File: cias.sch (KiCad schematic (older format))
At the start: 60 parts, among them CN13 KEYBOARD, CN6 DB25_Male, CN7 DB25_Female, Q501 2N3904, Q502 2N3906, Q503 2N3906, Q711 2N3904, U38 MC1488, U39 MC1489, U42 NE555, U7 VIA_8520, U8 VIA_8520

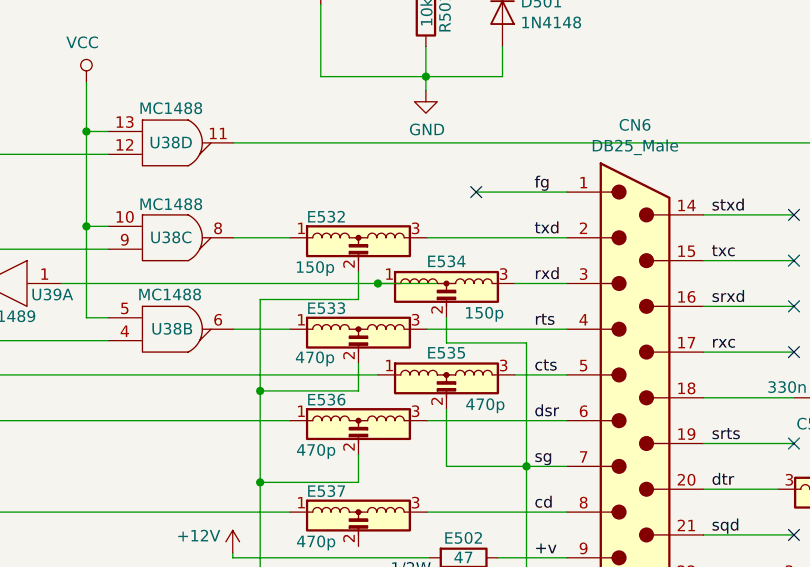
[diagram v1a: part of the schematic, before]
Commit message: Add expansion bus
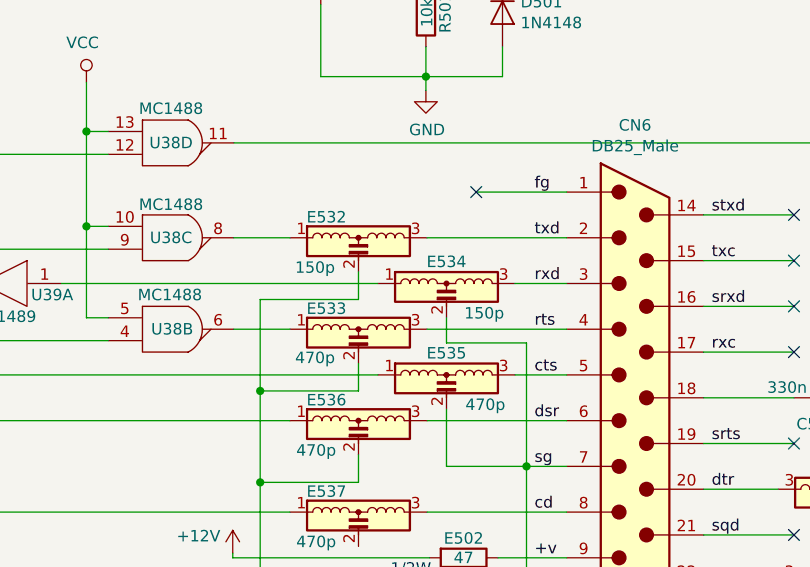
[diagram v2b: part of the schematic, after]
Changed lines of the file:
@@
 $Descr A3 16535 11693
 encoding utf-8
-Sheet 6 10
+Sheet 6 11
 Title "Rämixx500"
-Date "2019-04-17"
+Date "2019-04-20"
 Rev "1git"
 Comp "SukkoPera"
@@
 Wire Wire Line
 	7500 7010 7745 7010
-Connection ~ 8130 6810
-Wire Wire Line
-	8130 6810 8385 6810
 Wire Wire Line
 	6275 6245 6950 6245

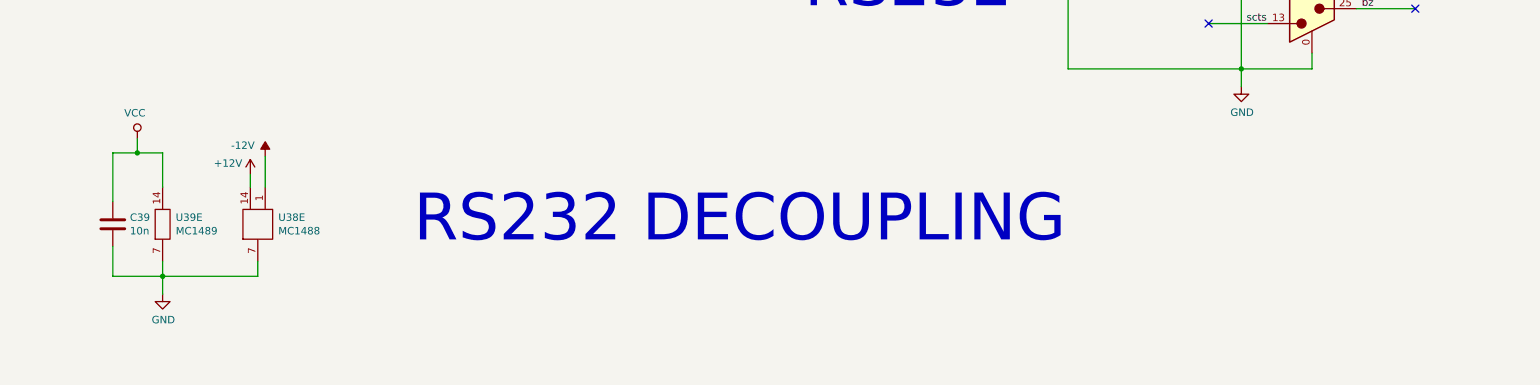
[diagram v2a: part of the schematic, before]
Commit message: Add power & decoupling, not yet complete
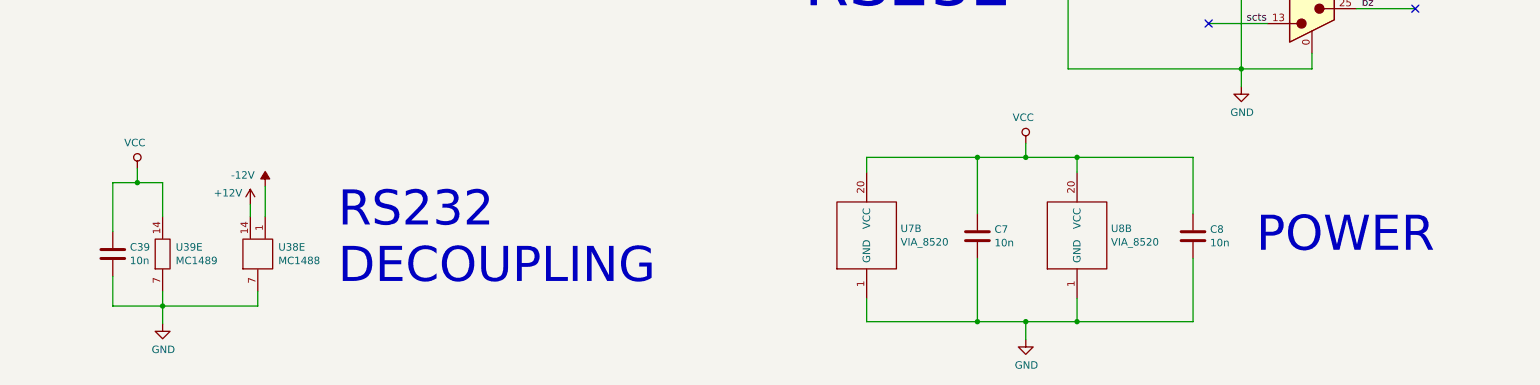
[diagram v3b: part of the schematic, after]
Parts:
- added C7, C8: 10n, symbol Device:C
- added unit 2 of U7
- added unit 2 of U8
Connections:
- net GND: now also C7.2, C8.2, U7.1 (GND), U8.1 (GND)
- net VCC: now also C7.1, C8.1, U7.20 (VCC), U8.20 (VCC)
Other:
- note added: "POWER"
- note added: "RS232\nDECOUPLING"
- note removed: "RS232 DECOUPLING"
- moved on the sheet: C39, U38E, U39E
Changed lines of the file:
@@
 $Descr A3 16535 11693
 encoding utf-8
-Sheet 6 11
+Sheet 6 12
 Title "Rämixx500"
 Date "2019-04-20"
@@
 L mc1489:MC1489 U39
 U 5 1 5F66BBE4
-P 1525 10160
-F 0 "U39" H 1613 10206 50  0000 L CNN
-F 1 "MC1489" H 1613 10115 50  0000 L CNN
-F 2 "Package_DIP:DIP-14_W7.62mm_Socket_LongPads" H 1525 9910 50  0001 C CNN
-F 3 "DOCUMENTATION" H 1525 9810 50  0001 C CNN
-	5    1525 10160
+P 1525 10360
+F 0 "U39" H 1613 10406 50  0000 L CNN
+F 1 "MC1489" H 1613 10315 50  0000 L CNN
+F 2 "Package_DIP:DIP-14_W7.62mm_Socket_LongPads" H 1525 10110 50  0001 C CNN
+F 3 "DOCUMENTATION" H 1525 10010 50  0001 C CNN
+	5    1525 10360
 	1    0    0    -1
 $EndComp
@@
 L MC1488:MC1488 U38
 U 5 1 5F687998
-P 2165 10160
-F 0 "U38" H 2303 10206 50  0000 L CNN
-F 1 "MC1488" H 2303 10115 50  0000 L CNN
-F 2 "Package_DIP:DIP-14_W7.62mm_Socket_LongPads" H 2165 9910 50  0001 C CNN
-F 3 "DOCUMENTATION" H 2165 9810 50  0001 C CNN
-	5    2165 10160
+P 2165 10360
+F 0 "U38" H 2303 10406 50  0000 L CNN
+F 1 "MC1488" H 2303 10315 50  0000 L CNN
+F 2 "Package_DIP:DIP-14_W7.62mm_Socket_LongPads" H 2165 10110 50  0001 C CNN
+F 3 "DOCUMENTATION" H 2165 10010 50  0001 C CNN
+	5    2165 10360
 	1    0    0    -1
 $EndComp
@@
 L Device:C C39
 U 1 1 5F6A3A58
-P 1190 10160
-F 0 "C39" H 1305 10206 50  0000 L CNN
-F 1 "10n" H 1305 10115 50  0000 L CNN
-F 2 "" H 1228 10010 50  0001 C CNN
-F 3 "~" H 1190 10160 50  0001 C CNN
-	1    1190 10160
-	1    0    0    -1
-$EndComp
-Wire Wire Line
-	1190 10310 1190 10510
-Wire Wire Line
-	1190 10510 1525 10510
-Wire Wire Line
-	2165 10510 2165 10410
-Wire Wire Line
-	1525 10410 1525 10510
-Connection ~ 1525 10510
-Wire Wire Line
-	1525 10510 2165 10510
+P 1190 10360
+F 0 "C39" H 1305 10406 50  0000 L CNN
+F 1 "10n" H 1305 10315 50  0000 L CNN
+F 2 "" H 1228 10210 50  0001 C CNN
+F 3 "~" H 1190 10360 50  0001 C CNN
+	1    1190 10360
+	1    0    0    -1
+$EndComp
+Wire Wire Line
+	1190 10510 1190 10710
+Wire Wire Line
+	1190 10710 1525 10710
+Wire Wire Line
+	2165 10710 2165 10610
+Wire Wire Line
+	1525 10610 1525 10710
+Connection ~ 1525 10710
+Wire Wire Line
+	1525 10710 2165 10710
 $Comp
 L power:GND #PWR0169
 U 1 1 5F6DC274
-P 1525 10630
-F 0 "#PWR0169" H 1525 10380 50  0001 C CNN
-F 1 "GND" H 1530 10457 50  0000 C CNN
-F 2 "" H 1525 10630 50  0001 C CNN
-F 3 "" H 1525 10630 50  0001 C CNN
-	1    1525 10630
-	1    0    0    -1
-$EndComp
-Wire Wire Line
-	1525 10630 1525 10510
-Wire Wire Line
-	1190 10010 1190 9680
-Wire Wire Line
-	1190 9680 1355 9680
-Wire Wire Line
-	1525 9680 1525 9910
+P 1525 10830
+F 0 "#PWR0169" H 1525 10580 50  0001 C CNN
+F 1 "GND" H 1530 10657 50  0000 C CNN
+F 2 "" H 1525 10830 50  0001 C CNN
+F 3 "" H 1525 10830 50  0001 C CNN
+	1    1525 10830
+	1    0    0    -1
+$EndComp
+Wire Wire Line
+	1525 10830 1525 10710
+Wire Wire Line
+	1190 10210 1190 9880
+Wire Wire Line
+	1190 9880 1355 9880
+Wire Wire Line
+	1525 9880 1525 10110
 $Comp
 L power:VCC #PWR0170
 U 1 1 5F715FB0
-P 1355 9585
-F 0 "#PWR0170" H 1355 9435 50  0001 C CNN
-F 1 "VCC" H 1372 9758 50  0000 C CNN
-F 2 "" H 1355 9585 50  0001 C CNN
-F 3 "" H 1355 9585 50  0001 C CNN
-	1    1355 9585
+P 1355 9785
+F 0 "#PWR0170" H 1355 9635 50  0001 C CNN
+F 1 "VCC" H 1372 9958 50  0000 C CNN
+F 2 "" H 1355 9785 50  0001 C CNN
+F 3 "" H 1355 9785 50  0001 C CNN
+	1    1355 9785
 	-1   0    0    -1
 $EndComp
 Wire Wire Line
-	1355 9680 1355 9585
-Connection ~ 1355 9680
-Wire Wire Line
-	1355 9680 1525 9680
+	1355 9880 1355 9785
+Connection ~ 1355 9880
+Wire Wire Line
+	1355 9880 1525 9880
 $Comp
 L power:+12V #PWR0171
 U 1 1 5F76EC3B
-P 2115 9825
-F 0 "#PWR0171" H 2115 9675 50  0001 C CNN
-F 1 "+12V" H 1965 9900 50  0000 C CNN
-F 2 "" H 2115 9825 50  0001 C CNN
-F 3 "" H 2115 9825 50  0001 C CNN
-	1    2115 9825
+P 2115 10025
+F 0 "#PWR0171" H 2115 9875 50  0001 C CNN
+F 1 "+12V" H 1965 10100 50  0000 C CNN
+F 2 "" H 2115 10025 50  0001 C CNN
+F 3 "" H 2115 10025 50  0001 C CNN
+	1    2115 10025
 	1    0    0    -1
 $EndComp
@@
 L power:-12V #PWR0172
 U 1 1 5F76ECA6
-P 2215 9705
-F 0 "#PWR0172" H 2215 9805 50  0001 C CNN
-F 1 "-12V" H 2065 9780 50  0000 C CNN
-F 2 "" H 2215 9705 50  0001 C CNN
-F 3 "" H 2215 9705 50  0001 C CNN
-	1    2215 9705
-	1    0    0    -1
-$EndComp
-Wire Wire Line
-	2215 9705 2215 9910
-Wire Wire Line
-	2115 9825 2115 9910
-Text Notes 7600 10310 2    315  ~ 0
-RS232 DECOUPLING
+P 2215 9905
+F 0 "#PWR0172" H 2215 10005 50  0001 C CNN
+F 1 "-12V" H 2065 9980 50  0000 C CNN
+F 2 "" H 2215 9905 50  0001 C CNN
+F 3 "" H 2215 9905 50  0001 C CNN
+	1    2215 9905
+	1    0    0    -1
+$EndComp
+Wire Wire Line
+	2215 9905 2215 10110
+Wire Wire Line
+	2115 10025 2115 10110
+Text Notes 2705 10580 0    236  ~ 0
+RS232\nDECOUPLING
 $Comp
 L Device:R R504
@@
 Text Label 1630 2260 0    50   ~ 0
 d[0..15]
+$Comp
+L VIA_8520:VIA_8520 U7
+U 2 1 5E9FA6CE
+P 6260 10260
+F 0 "U7" H 6488 10331 50  0000 L CNN
+F 1 "VIA_8520" H 6488 10240 50  0000 L CNN
+F 2 "Package_DIP:DIP-40_W15.24mm_Socket_LongPads" H 6260 10260 50  0001 C CNN
+F 3 "DOCUMENTATION" H 6260 10260 50  0001 C CNN
+	2    6260 10260
+	1    0    0    -1
+$EndComp
+$Comp
+L VIA_8520:VIA_8520 U8
+U 2 1 5EA251E0
+P 7675 10260
+F 0 "U8" H 7903 10331 50  0000 L CNN
+F 1 "VIA_8520" H 7903 10240 50  0000 L CNN
+F 2 "Package_DIP:DIP-40_W15.24mm_Socket_LongPads" H 7675 10260 50  0001 C CNN
+F 3 "DOCUMENTATION" H 7675 10260 50  0001 C CNN
+	2    7675 10260
+	1    0    0    -1
+$EndComp
+$Comp
+L Device:C C7
+U 1 1 5EA2573B
+P 7005 10240
+F 0 "C7" H 7120 10286 50  0000 L CNN
+F 1 "10n" H 7120 10195 50  0000 L CNN
+F 2 "" H 7043 10090 50  0001 C CNN
+F 3 "~" H 7005 10240 50  0001 C CNN
+	1    7005 10240
+	1    0    0    -1
+$EndComp
+$Comp
+L Device:C C8
+U 1 1 5EA25E9D
+P 8455 10240
+F 0 "C8" H 8570 10286 50  0000 L CNN
+F 1 "10n" H 8570 10195 50  0000 L CNN
+F 2 "" H 8493 10090 50  0001 C CNN
+F 3 "~" H 8455 10240 50  0001 C CNN
+	1    8455 10240
+	1    0    0    -1
+$EndComp
+Wire Wire Line
+	6260 9810 6260 9710
+Wire Wire Line
+	6260 9710 7005 9710
+Wire Wire Line
+	7675 9710 7675 9810
+Wire Wire Line
+	7005 10090 7005 9710
+Connection ~ 7005 9710
+Wire Wire Line
+	7005 9710 7330 9710
+Wire Wire Line
+	7675 9710 8455 9710
+Wire Wire Line
+	8455 9710 8455 10090
+Connection ~ 7675 9710
+Wire Wire Line
+	6260 10660 6260 10815
+Wire Wire Line
+	6260 10815 7005 10815
+Wire Wire Line
+	7675 10815 7675 10660
+Wire Wire Line
+	7675 10815 8455 10815
+Wire Wire Line
+	8455 10815 8455 10390
+Connection ~ 7675 10815
+Wire Wire Line
+	7005 10390 7005 10815
+Connection ~ 7005 10815
+Wire Wire Line
+	7005 10815 7330 10815
+$Comp
+L power:VCC #PWR0224
+U 1 1 5EB2D462
+P 7330 9615
+F 0 "#PWR0224" H 7330 9465 50  0001 C CNN
+F 1 "VCC" H 7347 9788 50  0000 C CNN
+F 2 "" H 7330 9615 50  0001 C CNN
+F 3 "" H 7330 9615 50  0001 C CNN
+	1    7330 9615
+	-1   0    0    -1
+$EndComp
+Wire Wire Line
+	7330 9710 7330 9615
+Connection ~ 7330 9710
+Wire Wire Line
+	7330 9710 7675 9710
+$Comp
+L power:GND #PWR0225
+U 1 1 5EB5B6F5
+P 7330 10935
+F 0 "#PWR0225" H 7330 10685 50  0001 C CNN
+F 1 "GND" H 7335 10762 50  0000 C CNN
+F 2 "" H 7330 10935 50  0001 C CNN
+F 3 "" H 7330 10935 50  0001 C CNN
+	1    7330 10935
+	1    0    0    -1
+$EndComp
+Wire Wire Line
+	7330 10935 7330 10815
+Connection ~ 7330 10815
+Wire Wire Line
+	7330 10815 7675 10815
+Text Notes 10080 10370 2    236  ~ 0
+POWER
 Wire Bus Line
 	1785 3110 1785 6275

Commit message: Add RTC
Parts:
- C712: footprint (none) -> Capacitor_THT:CP_Radial_D8.0mm_P5.00mm
- CN7: footprint w_conn_d-sub:DB_25F -> w_conn_d-sub:DB_25M
- D501: footprint (none) -> Diode_THT:D_DO-35_SOD27_P12.70mm_Horizontal
- JP1: footprint Jumper:SolderJumper-2_P1.3mm_Bridged_RoundedPad1.0x1.5mm -> Raemixx500:Jumper2-Bridged
- JP7B1: footprint Jumper:SolderJumper-3_P1.3mm_Bridged12_RoundedPad1.0x1.5mm_NumberLabels -> Raemixx500:Jumper3-Bridged12
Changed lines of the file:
@@
 $Descr A3 16535 11693
 encoding utf-8
-Sheet 6 12
+Sheet 6 13
 Title "Rämixx500"
 Date "2019-04-20"
@@
 F 0 "JP7B1" V 1240 4427 50  0000 L CNN
 F 1 "Jumper_3_Bridged12" V 1195 4426 50  0001 L CNN
-F 2 "Jumper:SolderJumper-3_P1.3mm_Bridged12_RoundedPad1.0x1.5mm_NumberLabels" H 1240 4360 50  0001 C CNN
+F 2 "Raemixx500:Jumper3-Bridged12" H 1240 4360 50  0001 C CNN
 F 3 "~" H 1240 4360 50  0001 C CNN
 	1    1240 4360
@@
 F 0 "CN7" H 9255 4082 50  0000 C CNN
 F 1 "DB25_Female" H 9255 3991 50  0000 C CNN
-F 2 "w_conn_d-sub:DB_25F" H 9255 2590 50  0001 C CNN
+F 2 "w_conn_d-sub:DB_25M" H 9255 2590 50  0001 C CNN
 F 3 " ~" H 9255 2590 50  0001 C CNN
 	1    9255 2590
@@
 F 0 "D501" V 8629 5704 50  0000 L CNN
 F 1 "1N4148" V 8720 5704 50  0000 L CNN
-F 2 "" H 8675 5450 50  0001 C CNN
+F 2 "Diode_THT:D_DO-35_SOD27_P12.70mm_Horizontal" H 8675 5450 50  0001 C CNN
 F 3 "http://www.nxp.com/documents/data_sheet/1N4148_1N4448.pdf" H 8675 5625 50  0001 C CNN
 	1    8675 5625
@@
 F 0 "C712" H 12405 7816 50  0000 L CNN
 F 1 "10u" H 12405 7725 50  0000 L CNN
-F 2 "" H 12328 7620 50  0001 C CNN
+F 2 "Capacitor_THT:CP_Radial_D8.0mm_P5.00mm" H 12328 7620 50  0001 C CNN
 F 3 "~" H 12290 7770 50  0001 C CNN
 	1    12290 7770
@@
 F 0 "JP1" H 14350 7238 50  0000 C CNN
 F 1 "Jumper_2_Bridged" H 14350 7239 50  0001 C CNN
-F 2 "Jumper:SolderJumper-2_P1.3mm_Bridged_RoundedPad1.0x1.5mm" H 14350 7135 50  0001 C CNN
+F 2 "Raemixx500:Jumper2-Bridged" H 14350 7135 50  0001 C CNN
 F 3 "~" H 14350 7135 50  0001 C CNN
 	1    14350 7135

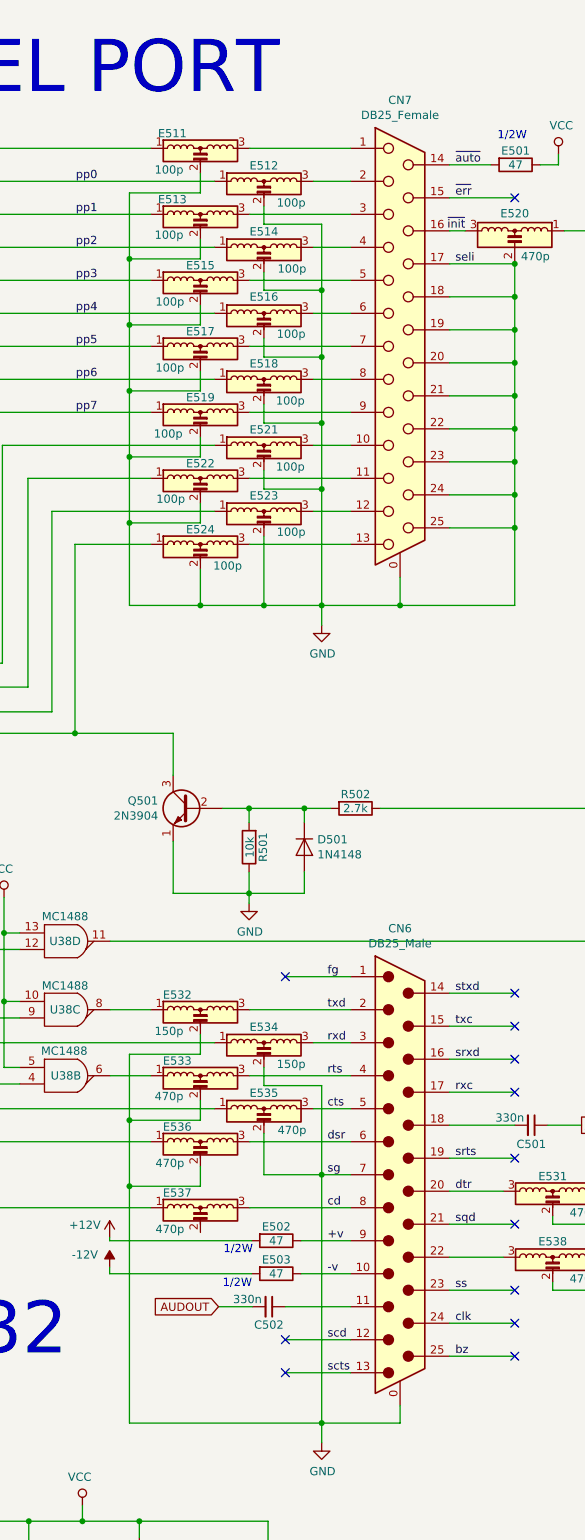
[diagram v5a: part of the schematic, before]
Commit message: Add external floppy connector (and do a few fixes)
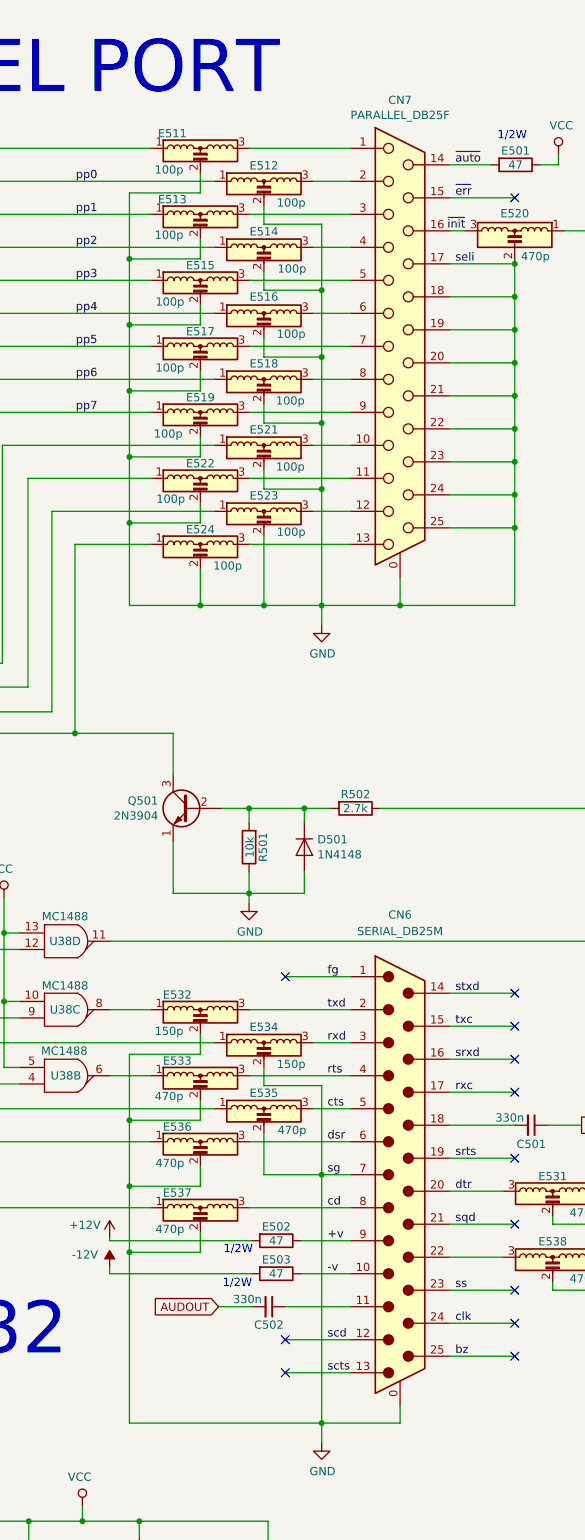
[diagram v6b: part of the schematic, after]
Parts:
- CN6: value DB25_Male -> SERIAL_DB25M
- CN7: value DB25_Female -> PARALLEL_DB25F
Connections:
- net GND: now also E537.2
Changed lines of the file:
@@
 P 9255 2590
 F 0 "CN7" H 9255 4082 50  0000 C CNN
-F 1 "DB25_Female" H 9255 3991 50  0000 C CNN
+F 1 "PARALLEL_DB25F" H 9255 3991 50  0000 C CNN
 F 2 "w_conn_d-sub:DB_25M" H 9255 2590 50  0001 C CNN
 F 3 " ~" H 9255 2590 50  0001 C CNN
@@
 U 1 1 5EBF2D7E
 P 9255 7610
-F 0 "CN6" H 9255 6118 50  0000 C CNN
-F 1 "DB25_Male" H 9255 6209 50  0000 C CNN
+F 0 "CN6" H 9255 6035 50  0000 C CNN
+F 1 "SERIAL_DB25M" H 9255 6135 50  0000 C CNN
 F 2 "w_conn_d-sub:DB_25M" H 9255 7610 50  0001 C CNN
 F 3 " ~" H 9255 7610 50  0001 C CNN
@@
 Connection ~ 7615 7680
 Wire Wire Line
-	7615 7680 7615 9115
+	7615 7680 7615 8080
 Wire Wire Line
 	8780 9115 7615 9115
@@
 Text Notes 10080 10370 2    236  ~ 0
 POWER
+Wire Wire Line
+	8045 7960 8045 8080
+Wire Wire Line
+	8045 8080 7615 8080
+Connection ~ 7615 8080
+Wire Wire Line
+	7615 8080 7615 9115
 Wire Bus Line
 	1785 3110 1785 6275
